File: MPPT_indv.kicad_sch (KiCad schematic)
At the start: 21 parts, among them Q10 NMOS, Q9 NMOS, U17 LTC4162IUFD-LADM_PBF

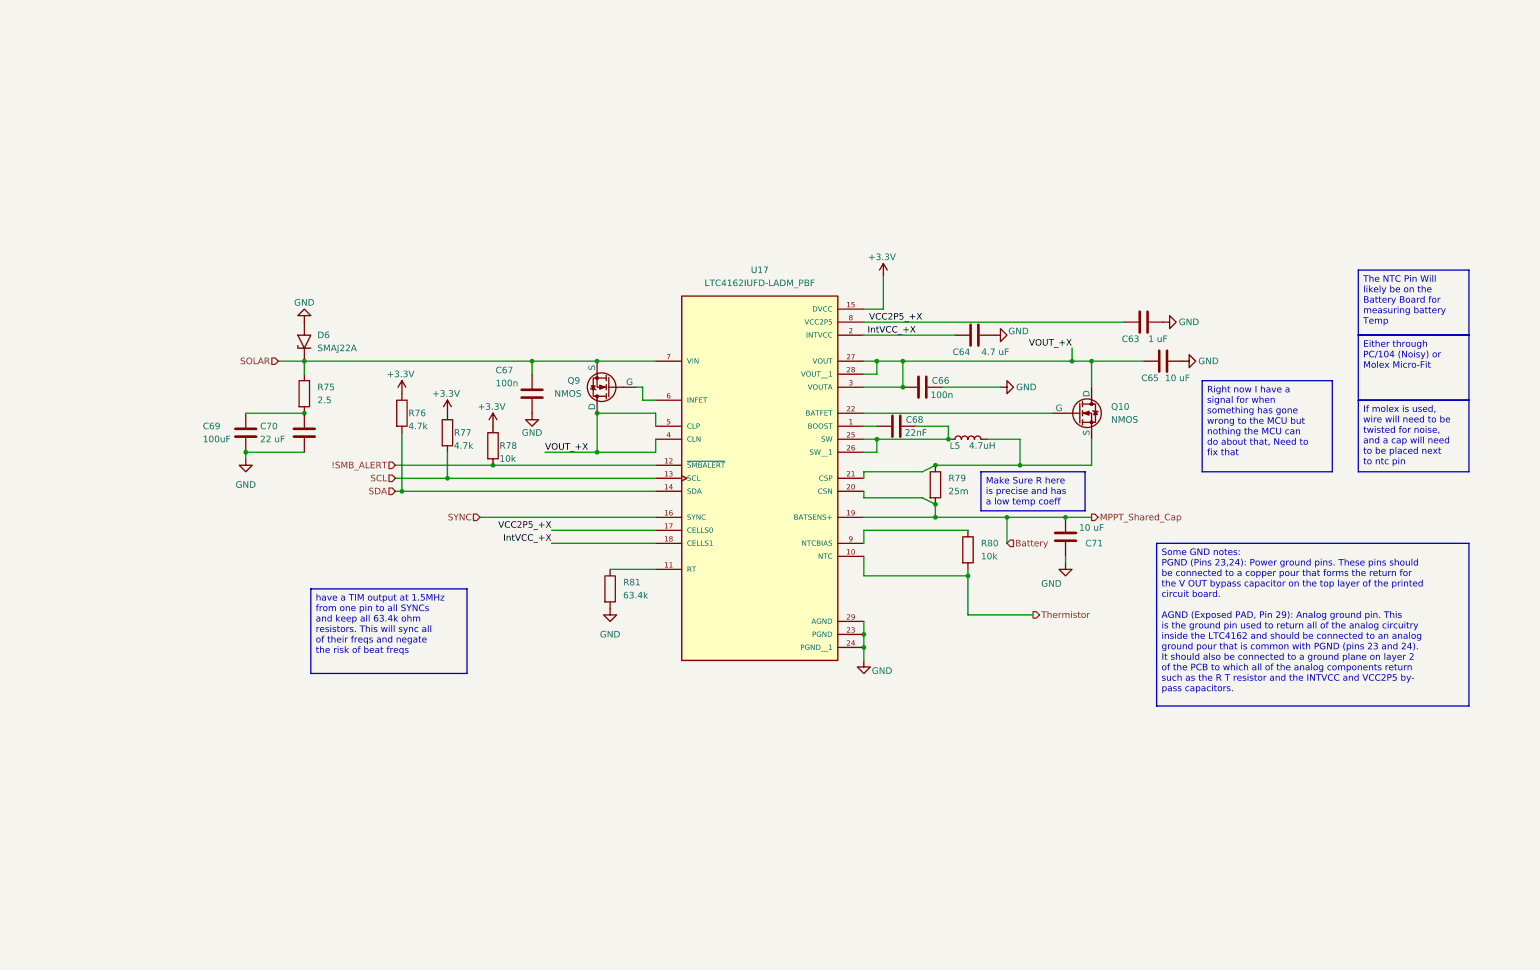
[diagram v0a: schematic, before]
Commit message: Small schematic changes
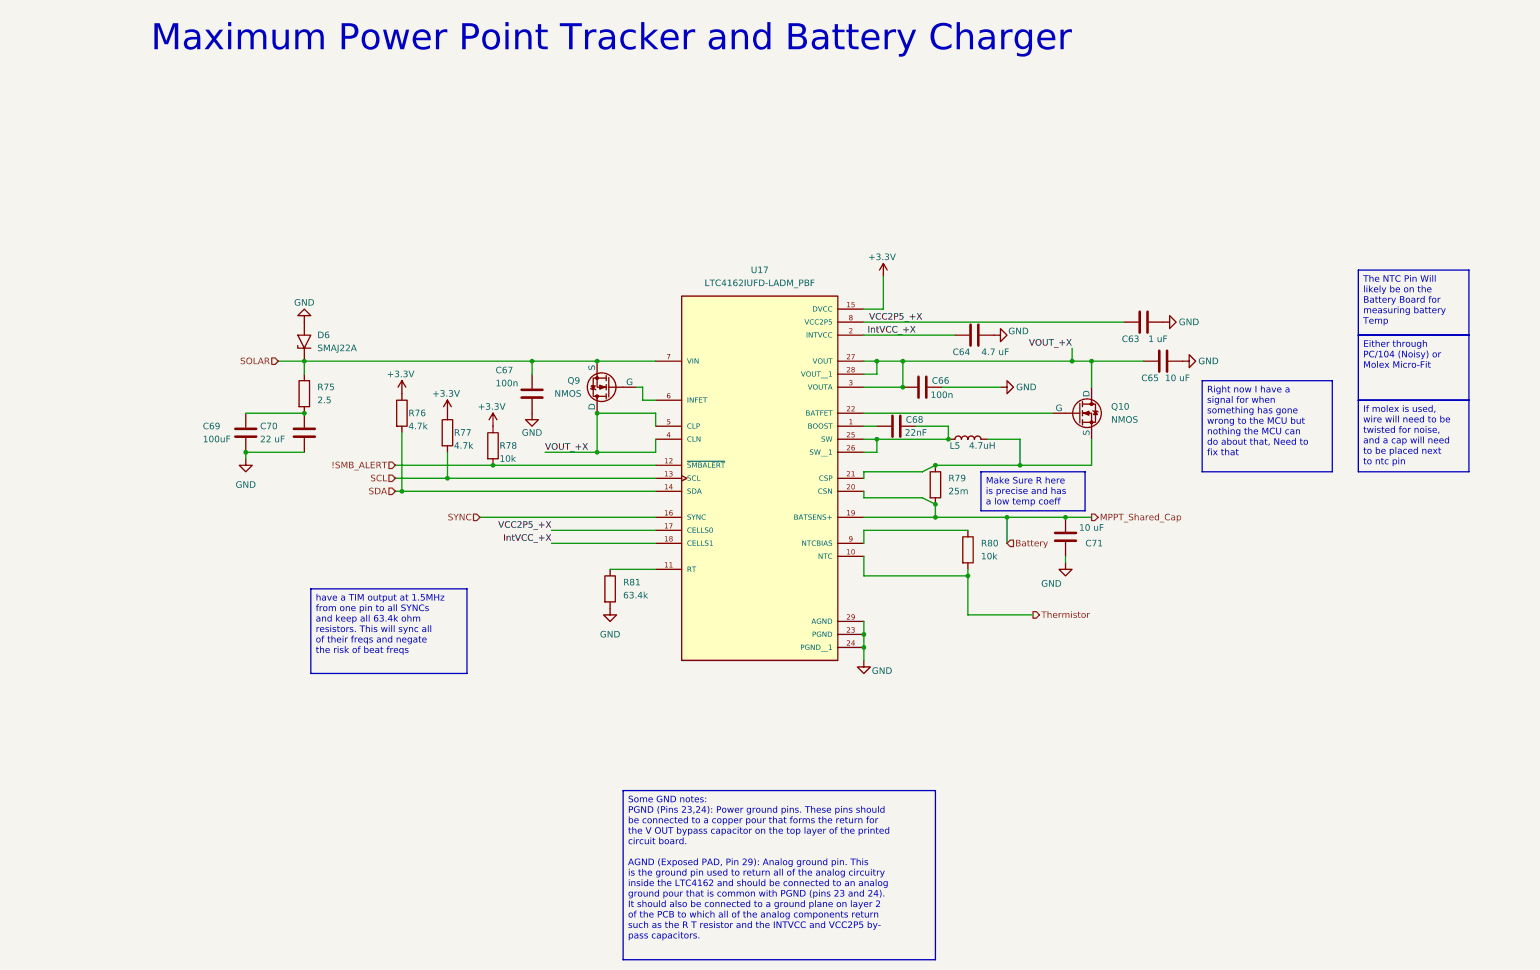
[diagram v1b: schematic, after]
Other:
- note added: "Maximum Power Point Tracker and Battery Charger"
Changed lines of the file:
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@@
 	(generator_version "9.0")
 	(paper "A4")
+	(text "Maximum Power Point Tracker and Battery Charger"
+		(exclude_from_sim no)
+		(at 113.284 18.288 0)
+		(effects
+			(font
+				(size 5.08 5.08)
+			)
+		)
+	)
 	(text_box "The NTC Pin Will likely be on the Battery Board for measuring battery Temp"
 		(exclude_from_sim no)
@@
 	(text_box "Some GND notes:\nPGND (Pins 23,24): Power ground pins. These pins should\nbe connected to a copper pour that forms the return for\nthe V OUT bypass capacitor on the top layer of the printed\ncircuit board.\n\nAGND (Exposed PAD, Pin 29): Analog ground pin. This\nis the ground pin used to return all of the analog circuitry\ninside the LTC4162 and should be connected to an analog\nground pour that is common with PGND (pins 23 and 24).\nIt should also be connected to a ground plane on layer 2\nof the PCB to which all of the analog components return\nsuch as the R T resistor and the INTVCC and VCC2P5 by-\npass capacitors."
 		(exclude_from_sim no)
-		(at 219.71 116.84 0)
-		(size 60.96 31.75)
+		(at 115.57 165.1 0)
+		(size 60.96 33.02)
 		(margins 0.9525 0.9525 0.9525 0.9525)
 		(stroke

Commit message: Changed LTC 4412 to 4417, still kinks to work out
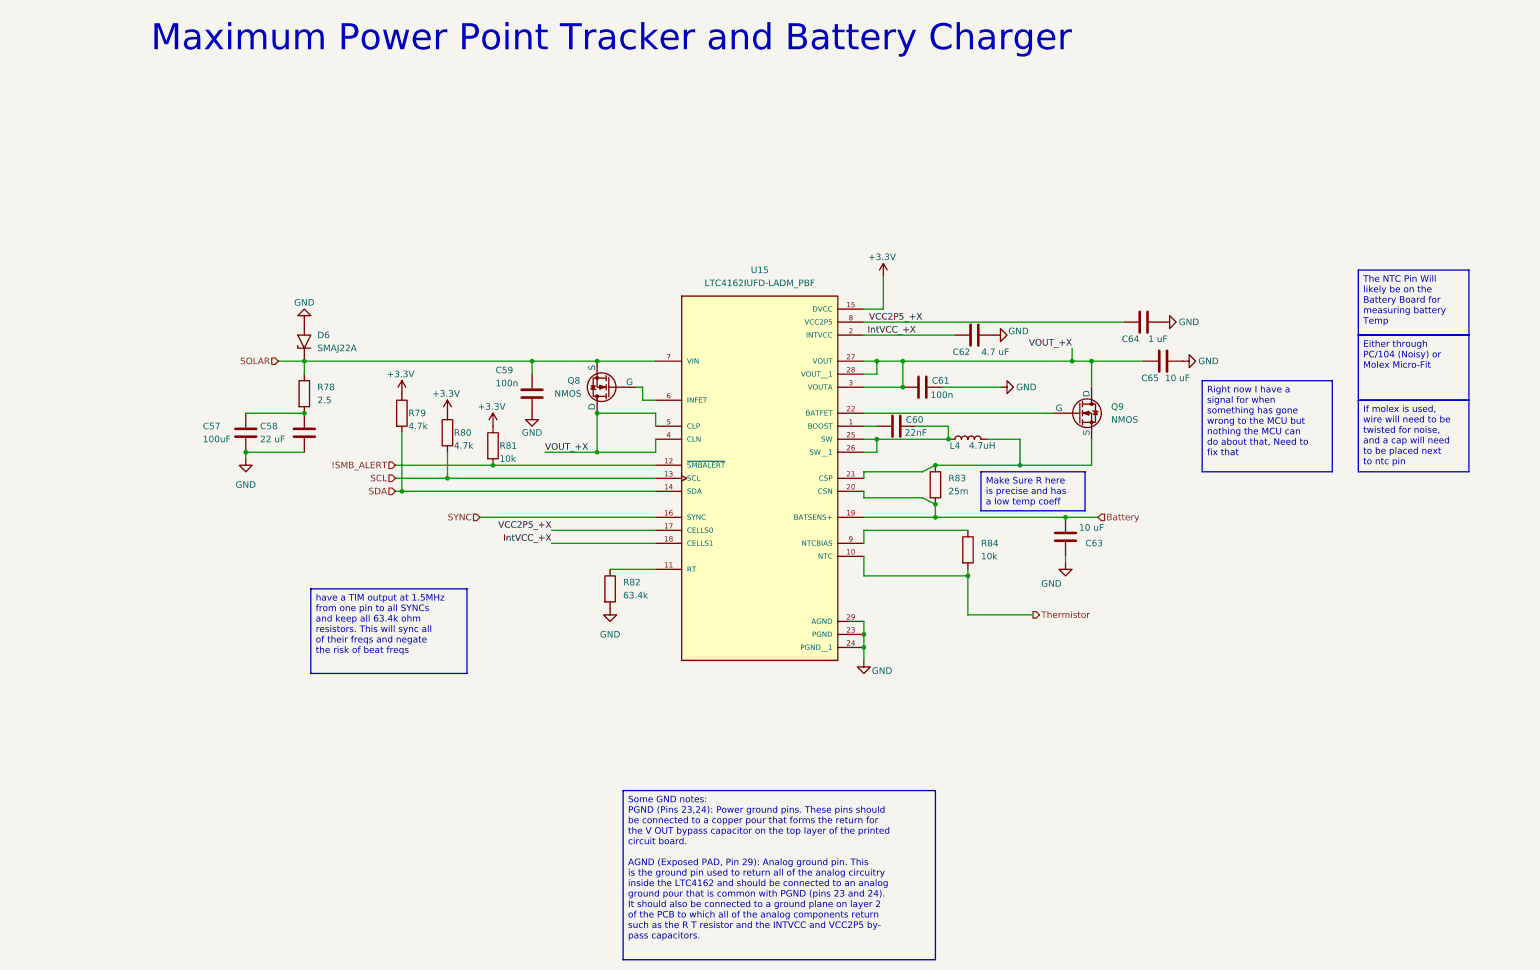
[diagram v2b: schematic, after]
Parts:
- Q8: renamed from Q9; footprint Package_TO_SOT_SMD:LFPAK56 -> Package_TO_SOT_SMD:TSOT-23; MANUFACTURER (none) -> Digikey; MANUFACTURER_PART_NUMBER PSMN4R0-40YS,115 -> AO3400A
- Q9: renamed from Q10; footprint Package_TO_SOT_SMD:LFPAK56 -> Package_TO_SOT_SMD:TSOT-23; MANUFACTURER (none) -> Digikey; MANUFACTURER_PART_NUMBER PSMN4R0-40YS,115 -> AO3400A
- renumbered C69 to C57, C70 to C58, C67 to C59, C68 to C60, C66 to C61, C64 to C62, C71 to C63, C63 to C64, L5 to L4, R75 to R78, R76 to R79, R77 to R80, R78 to R81, R81 to R82, R79 to R83, R80 to R84, U17 to U15

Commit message: Started PCB layout
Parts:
- added R82: 10m, Resistor_SMD:R_0815_2038Metric, symbol Device:R
- D6: MANUFACTURER DigiKey -> (none)
- R83: renamed from R82; value 63.4k -> 44.2k; MANUFACTURER_PART_NUMBER RQ73C1J63K4BTD -> (none)
- renumbered R83 to R84, R84 to R85
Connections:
- net VOUT_+X: now also R82.2; no longer Q8.1 (D), U15.5 (CLP)
- net Battery renamed OUTPUT
- new net: Q8.1 (D), R82.1, U15.5 (CLP)
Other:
- moved on the sheet: C57, C58, R78
